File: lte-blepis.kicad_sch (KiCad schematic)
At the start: 82 parts, among them J1 MODEM_USB, J53 EXP, Q1 NPN, Q2 NPN, Q3 NPN, Q4 NPN, SW1 EVQPUL02K, SW2 EVQPUL02K, SW3 EVQPUL02K, U1 A7682E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

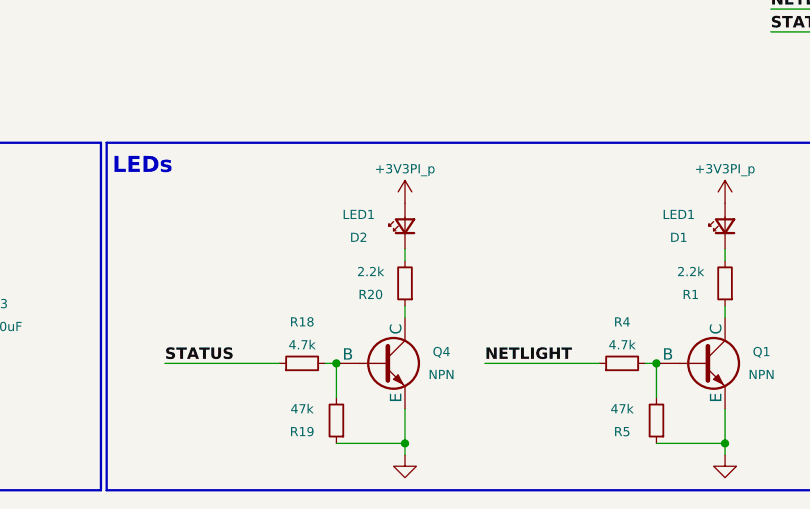
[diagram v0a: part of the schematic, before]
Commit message: refactor: flip design, flip footprints, re-do routing
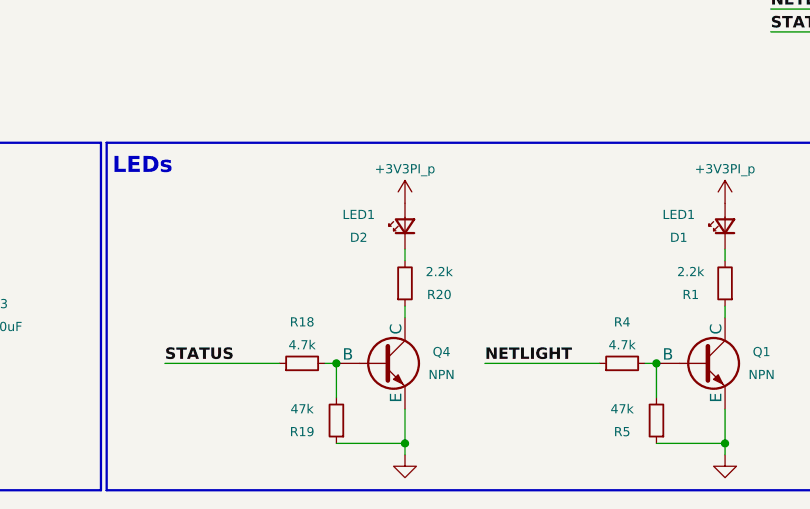
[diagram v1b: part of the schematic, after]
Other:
- moved on the sheet: R20
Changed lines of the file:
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@@
 		(lib_name "R_Small_1")
 		(lib_id "Device:R_Small")
-		(at 176.53 260.35 180)
+		(at 176.53 260.35 0)
+		(mirror x)
 		(unit 1)
 		(exclude_from_sim no)
@@
 		(dnp no)
 		(property "Reference" "R20"
-			(at 172.72 261.62 0)
+			(at 180.34 261.62 0)
 			(effects
 				(font
@@
 		)
 		(property "Value" "2.2k"
-			(at 172.72 259.08 0)
+			(at 180.34 259.08 0)
 			(effects
 				(font

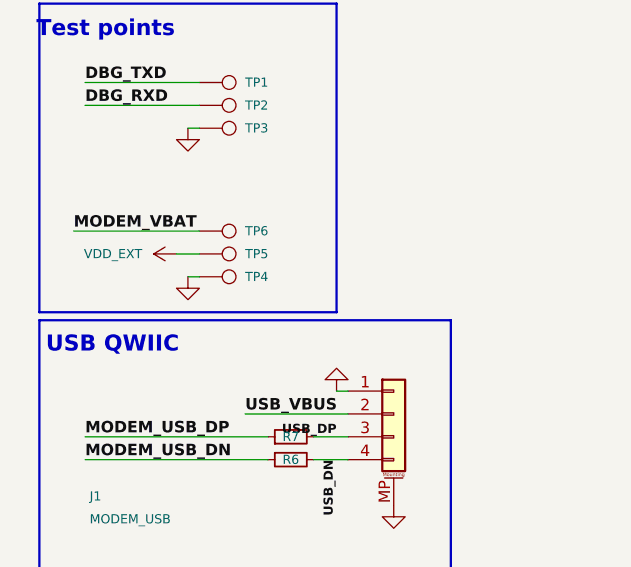
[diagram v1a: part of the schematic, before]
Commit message: tidy up test points and traces
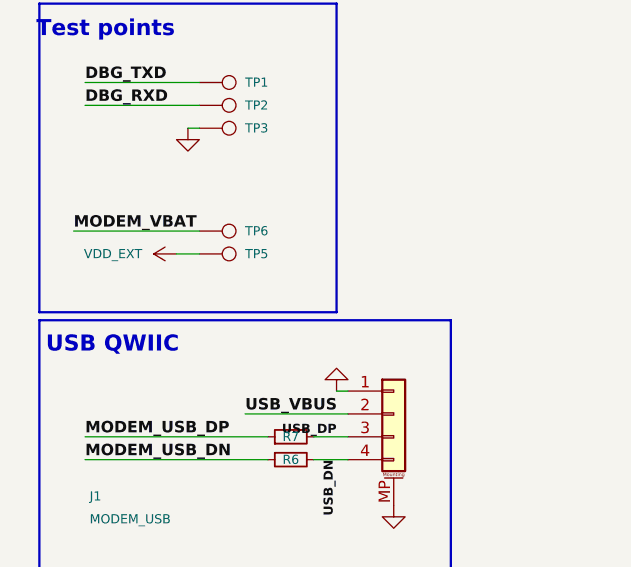
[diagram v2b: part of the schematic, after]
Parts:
- removed TP4: TestPoint, TestPoint:TestPoint_Pad_D2.5mm, symbol Connector:TestPoint
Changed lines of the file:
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@@
 	(wire
 		(pts
-			(xy 30.48 210.82) (xy 31.75 210.82)
-		)
-		(stroke
-			(width 0)
-			(type default)
-		)
-	)
-	(wire
-		(pts
 			(xy 36.83 90.17) (xy 36.83 88.9)
 		)
@@
 	)
 	(symbol
-		(lib_name "GND_3")
-		(lib_id "power:GND")
-		(at 30.48 210.82 0)
-		(unit 1)
-		(exclude_from_sim no)
-		(in_bom yes)
-		(on_board yes)
-		(dnp no)
-		(fields_autoplaced yes)
-		(property "Reference" "#PWR034"
-			(at 30.48 217.17 0)
-			(effects
-				(font
-					(size 1.016 1.016)
-				)
-				(hide yes)
-			)
-		)
-		(property "Value" "GND"
-			(at 30.48 215.9 0)
-			(effects
-				(font
-					(size 1.016 1.016)
-				)
-				(hide yes)
-			)
-		)
-		(property "Footprint" ""
-			(at 30.48 210.82 0)
-			(effects
-				(font
-					(size 1.27 1.27)
-				)
-				(hide yes)
-			)
-		)
-		(property "Datasheet" ""
-			(at 30.48 210.82 0)
-			(effects
-				(font
-					(size 1.27 1.27)
-				)
-				(hide yes)
-			)
-		)
-		(property "Description" "Power symbol creates a global label with name \"GND\" , ground"
-			(at 30.48 210.82 0)
-			(effects
-				(font
-					(size 1.27 1.27)
-				)
-				(hide yes)
-			)
-		)
-		(pin "1"
-		)
-		(instances
-			(project "lte-blepis"
-				(path "/aa18ae61-e3ae-45ea-87bb-2047657064f6"
-					(reference "#PWR034")
-					(unit 1)
-				)
-			)
-		)
-	)
-	(symbol
 		(lib_id "power:VDD")
 		(at 151.13 21.59 0)
@@
 					(unit 1)
 				)
-			)
-		)
-	)
-	(symbol
-		(lib_id "Connector:TestPoint")
-		(at 31.75 210.82 270)
-		(unit 1)
-		(exclude_from_sim no)
-		(in_bom yes)
-		(on_board yes)
-		(dnp no)
-		(property "Reference" "TP4"
-			(at 36.83 210.82 90)
-			(effects
-				(font
-					(size 1.016 1.016)
-				)
-				(justify left)
-			)
-		)
-		(property "Value" "TestPoint"
-			(at 36.83 212.0899 90)
-			(effects
-				(font
-					(size 1.016 1.016)
-				)
-				(justify left)
-				(hide yes)
-			)
-		)
-		(property "Footprint" "TestPoint:TestPoint_Pad_D2.5mm"
-			(at 31.75 215.9 0)
-			(effects
-				(font
-					(size 1.27 1.27)
-				)
-				(hide yes)
-			)
-		)
-		(property "Datasheet" "~"
-			(at 31.75 215.9 0)
-			(effects
-				(font
-					(size 1.27 1.27)
-				)
-				(hide yes)
-			)
-		)
-		(property "Description" "test point"
-			(at 31.75 210.82 0)
-			(effects
-				(font
-					(size 1.27 1.27)
-				)
-				(hide yes)
-			)
-		)
-		(pin "1"
-		)
-		(instances
-			(project "lte-blepis"
-				(path "/aa18ae61-e3ae-45ea-87bb-2047657064f6"
-					(reference "TP4")
-					(unit 1)
-				)
